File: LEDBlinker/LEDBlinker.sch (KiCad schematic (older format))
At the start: 7 parts

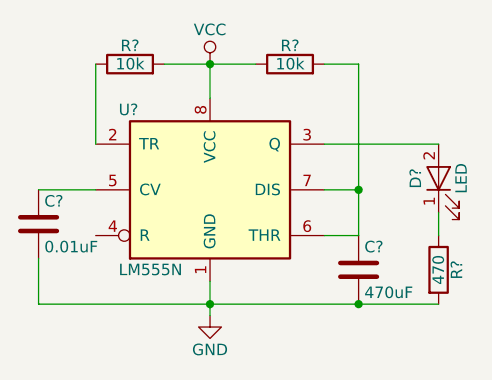
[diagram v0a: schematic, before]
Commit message: Finish schematic
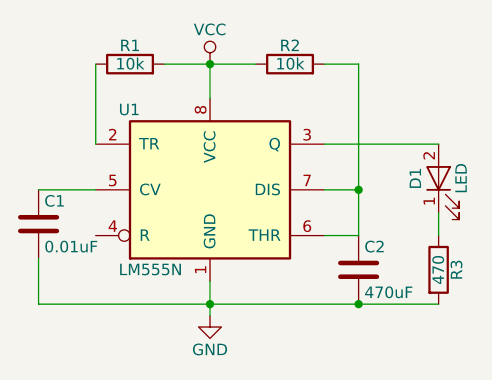
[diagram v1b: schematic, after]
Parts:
- C1, C2: renamed from C?; footprint (none) -> Capacitors_THT:CP_Axial_L10.0mm_D4.5mm_P15.00mm_Horizontal
- D1: renamed from D?; footprint (none) -> LEDs:LED-5MM
- R1, R2, R3: renamed from R?; footprint (none) -> Resistors_THT:Resistor_Horizontal_RM7mm
- U1: renamed from U?; footprint (none) -> Housings_DIP:DIP-8_W7.62mm_Socket
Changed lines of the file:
@@
 $EndDescr
 $Comp
-L LM555N U?
+L LM555N U1
 U 1 1 58FA4242
 P 5000 2800
-F 0 "U?" H 4600 3150 50  0000 L CNN
+F 0 "U1" H 4600 3150 50  0000 L CNN
 F 1 "LM555N" H 4600 2450 50  0000 L CNN
-F 2 "" H 5000 2800 50  0001 C CNN
+F 2 "Housings_DIP:DIP-8_W7.62mm_Socket" H 5000 2800 50  0001 C CNN
 F 3 "" H 5000 2800 50  0001 C CNN
 	1    5000 2800
@@
 $EndComp
 $Comp
-L R R?
+L R R2
 U 1 1 58FA43AD
 P 5350 2250
-F 0 "R?" V 5430 2250 50  0000 C CNN
+F 0 "R2" V 5430 2250 50  0000 C CNN
 F 1 "10k" V 5350 2250 50  0000 C CNN
-F 2 "" V 5280 2250 50  0001 C CNN
+F 2 "Resistors_THT:Resistor_Horizontal_RM7mm" V 5280 2250 50  0001 C CNN
 F 3 "" H 5350 2250 50  0001 C CNN
 	1    5350 2250
@@
 $EndComp
 $Comp
-L R R?
+L R R1
 U 1 1 58FA44E7
 P 4650 2250
-F 0 "R?" V 4730 2250 50  0000 C CNN
+F 0 "R1" V 4730 2250 50  0000 C CNN
 F 1 "10k" V 4650 2250 50  0000 C CNN
-F 2 "" V 4580 2250 50  0001 C CNN
+F 2 "Resistors_THT:Resistor_Horizontal_RM7mm" V 4580 2250 50  0001 C CNN
 F 3 "" H 4650 2250 50  0001 C CNN
 	1    4650 2250
@@
 $EndComp
 $Comp
-L R R?
+L R R3
 U 1 1 58FA458E
 P 6000 3150
-F 0 "R?" V 6080 3150 50  0000 C CNN
+F 0 "R3" V 6080 3150 50  0000 C CNN
 F 1 "470" V 6000 3150 50  0000 C CNN
-F 2 "" V 5930 3150 50  0001 C CNN
+F 2 "Resistors_THT:Resistor_Horizontal_RM7mm" V 5930 3150 50  0001 C CNN
 F 3 "" H 6000 3150 50  0001 C CNN
 	1    6000 3150
@@
 $EndComp
 $Comp
-L C C?
+L C C1
 U 1 1 58FA45B9
 P 4250 2950
-F 0 "C?" H 4275 3050 50  0000 L CNN
+F 0 "C1" H 4275 3050 50  0000 L CNN
 F 1 "0.01uF" H 4275 2850 50  0000 L CNN
-F 2 "" H 4288 2800 50  0001 C CNN
+F 2 "Capacitors_THT:CP_Axial_L10.0mm_D4.5mm_P15.00mm_Horizontal" H 4288 2800 50  0001 C CNN
 F 3 "" H 4250 2950 50  0001 C CNN
 	1    4250 2950
@@
 $EndComp
 $Comp
-L C C?
+L C C2
 U 1 1 58FA462D
 P 5650 3150
-F 0 "C?" H 5675 3250 50  0000 L CNN
+F 0 "C2" H 5675 3250 50  0000 L CNN
 F 1 "470uF" H 5675 3050 50  0000 L CNN
-F 2 "" H 5688 3000 50  0001 C CNN
+F 2 "Capacitors_THT:CP_Axial_L10.0mm_D4.5mm_P15.00mm_Horizontal" H 5688 3000 50  0001 C CNN
 F 3 "" H 5650 3150 50  0001 C CNN
 	1    5650 3150
@@
 $EndComp
 $Comp
-L LED D?
+L LED D1
 U 1 1 58FA4660
 P 6000 2750
-F 0 "D?" H 6000 2850 50  0000 C CNN
+F 0 "D1" H 6000 2850 50  0000 C CNN
 F 1 "LED" H 6000 2650 50  0000 C CNN
-F 2 "" H 6000 2750 50  0001 C CNN
+F 2 "LEDs:LED-5MM" H 6000 2750 50  0001 C CNN
 F 3 "" H 6000 2750 50  0001 C CNN
 	1    6000 2750
@@
 $EndComp
 $Comp
-L VCC #PWR?
+L VCC #PWR01
 U 1 1 58FA655A
 P 5000 2250
-F 0 "#PWR?" H 5000 2100 50  0001 C CNN
+F 0 "#PWR01" H 5000 2100 50  0001 C CNN
 F 1 "VCC" H 5000 2400 50  0000 C CNN
 F 2 "" H 5000 2250 50  0001 C CNN
@@
 $EndComp
 $Comp
-L GND #PWR?
+L GND #PWR02
 U 1 1 58FA6583
 P 5000 3350
-F 0 "#PWR?" H 5000 3100 50  0001 C CNN
+F 0 "#PWR02" H 5000 3100 50  0001 C CNN
 F 1 "GND" H 5000 3200 50  0000 C CNN
 F 2 "" H 5000 3350 50  0001 C CNN
@@
 $EndComp
 Wire Wire Line
-	5000 3200 5000 3300
-Wire Wire Line
-	5000 3300 5000 3350
+	5000 3200 5000 3350
 Wire Wire Line
 	5000 2250 5000 2400
 Wire Wire Line
-	4800 2250 5000 2250
-Wire Wire Line
-	5000 2250 5200 2250
+	4800 2250 5200 2250
 Connection ~ 5000 2250
 Wire Wire Line
@@
 	4250 3100 4250 3300
 Wire Wire Line
-	4250 3300 5000 3300
-Wire Wire Line
-	5000 3300 5650 3300
-Wire Wire Line
-	5650 3300 6000 3300
+	4250 3300 6000 3300
 Connection ~ 5000 3300
 Wire Wire Line
@@
 	5500 2250 5650 2250
 Wire Wire Line
-	5650 2250 5650 2800
+	5650 2250 5650 3000
 Wire Wire Line
-	5500 2800 5650 2800
-Wire Wire Line
-	5650 2800 5650 2800
-Wire Wire Line
-	5650 2800 5650 3000
+	5650 2800 5500 2800
 Connection ~ 5650 2800
 $EndSCHEMATC

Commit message: Functional complete first draft
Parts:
- C1, C2: footprint Capacitors_THT:CP_Axial_L10.0mm_D4.5mm_P15.00mm_Horizontal -> Capacitors_THT:C_Radial_D5_L6_P2.5
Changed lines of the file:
@@
 F 0 "C1" H 4275 3050 50  0000 L CNN
 F 1 "0.01uF" H 4275 2850 50  0000 L CNN
-F 2 "Capacitors_THT:CP_Axial_L10.0mm_D4.5mm_P15.00mm_Horizontal" H 4288 2800 50  0001 C CNN
+F 2 "Capacitors_THT:C_Radial_D5_L6_P2.5" H 4288 2800 50  0001 C CNN
 F 3 "" H 4250 2950 50  0001 C CNN
 	1    4250 2950
@@
 F 0 "C2" H 5675 3250 50  0000 L CNN
 F 1 "470uF" H 5675 3050 50  0000 L CNN
-F 2 "Capacitors_THT:CP_Axial_L10.0mm_D4.5mm_P15.00mm_Horizontal" H 5688 3000 50  0001 C CNN
+F 2 "Capacitors_THT:C_Radial_D5_L6_P2.5" H 5688 3000 50  0001 C CNN
 F 3 "" H 5650 3150 50  0001 C CNN
 	1    5650 3150
